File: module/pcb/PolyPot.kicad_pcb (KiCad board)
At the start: 2 copper layers, 50 x 50 mm, 40 parts, among them J1 V_BAT_1S, J2 PROG/DEBUG, J3 HUMIDITY_CONN, J4 TOF_DIST_SENS, J5 M3, J6 M3, J7 M3, J8 M3, J9 LUMINOSITY_CONN, M1 DC_WATER_PUMP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

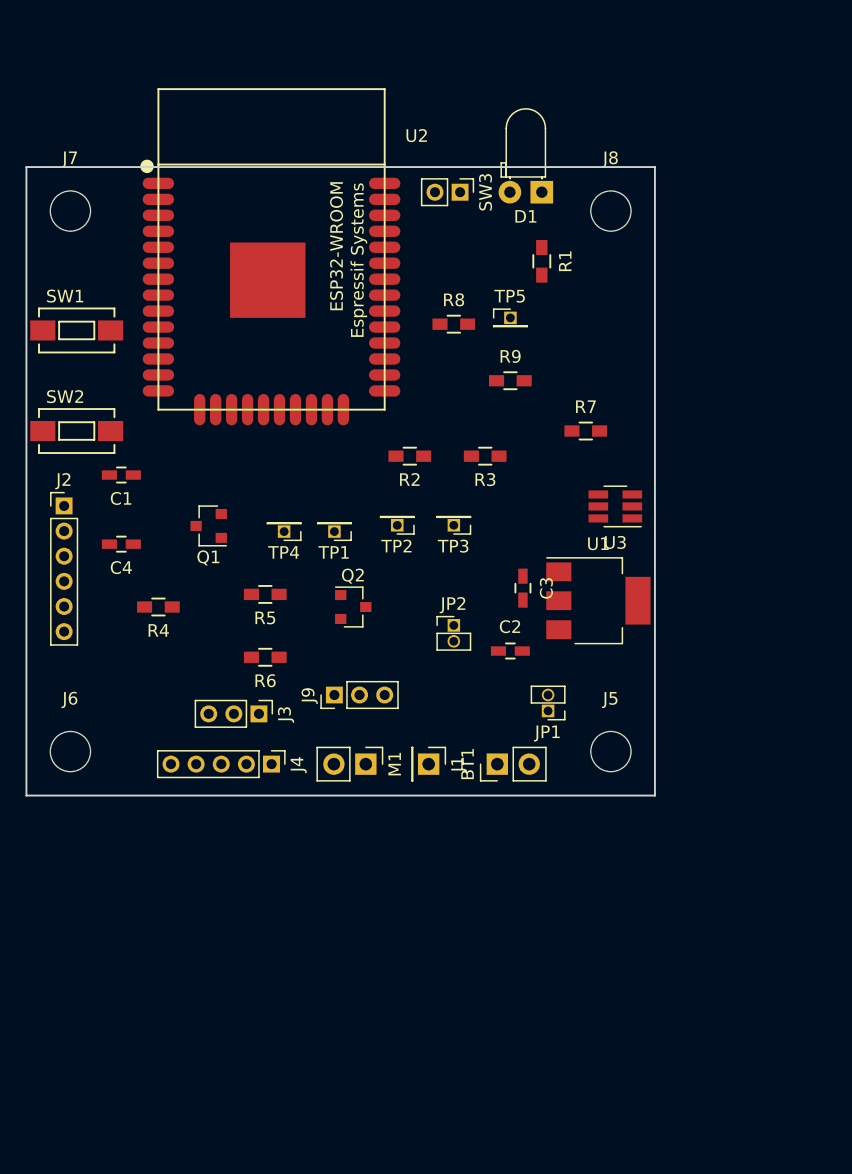
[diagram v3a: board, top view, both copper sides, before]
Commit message: First PCB routage+ small correction int the schematics
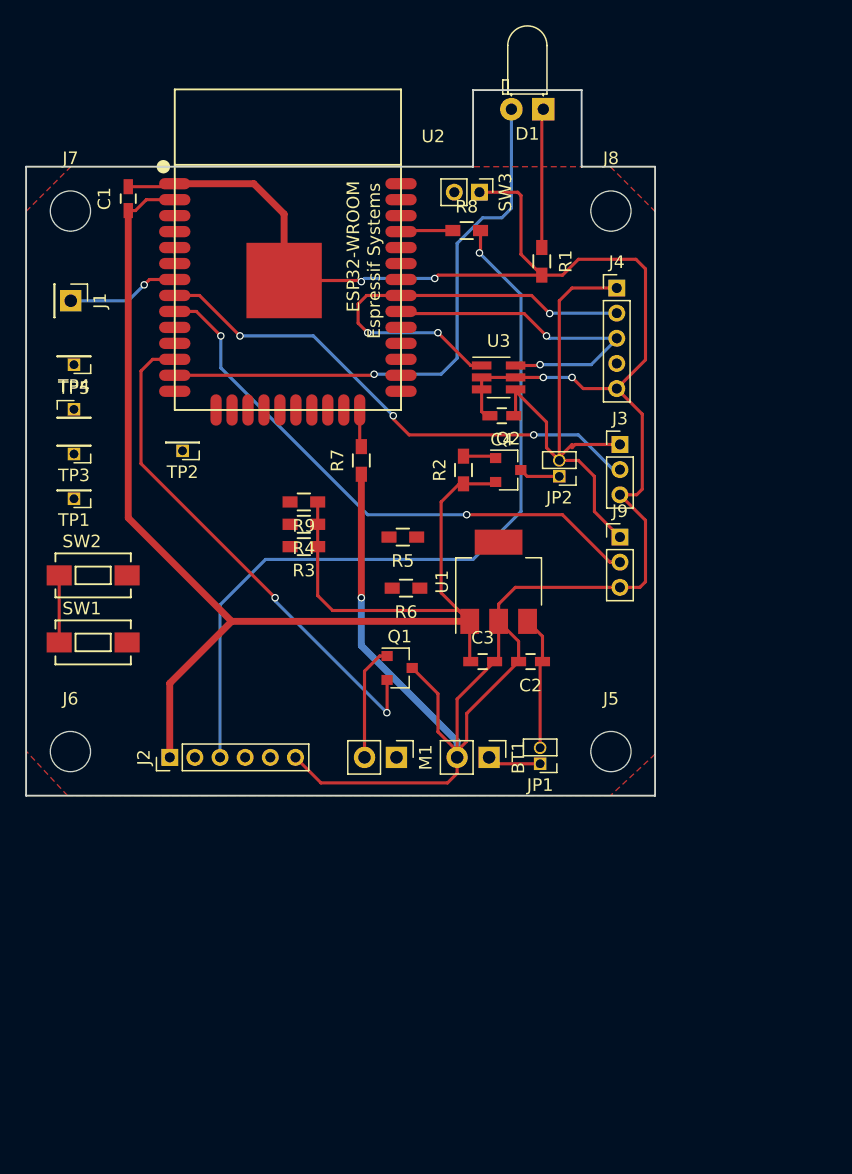
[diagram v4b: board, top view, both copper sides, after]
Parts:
- moved J4 46.8 mm to (77.0, 39.6), turned to 0 degrees
- moved J1 46.6 mm to (33.5, 40.6)
- moved J3 35.8 mm to (77.2, 52.1), turned to 0 degrees
- moved TP5 35.5 mm to (33.8, 49.3)
- moved C4 31.9 mm to (67.8, 49.8)
- moved TP3 30.7 mm to (33.8, 52.8)
- moved J9 26.0 mm to (77.2, 59.4), turned to 0 degrees
- moved SW1 24.9 mm to (35.3, 67.8)
- moved C1 22.0 mm to (38.1, 32.5), turned to 90 degrees
- moved J2 21.7 mm to (41.4, 77.0), turned to 90 degrees
- moved TP4 21.4 mm to (33.8, 45.7)
- moved TP1 20.9 mm to (33.8, 56.4)
- moved R9 19.1 mm to (52.1, 56.6), turned to 180 degrees
- moved Q1 18.9 mm to (59.7, 69.8), turned to 0 degrees
- moved TP2 18.1 mm to (42.4, 52.6)
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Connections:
- J4 pad 4: (no net) -> /TOF_GPIO0
- J5 pad 1: (no net) -> Net-(J5-Pad1)
- J6 pad 1: (no net) -> Net-(J6-Pad1)
- J7 pad 1: (no net) -> Net-(J7-Pad1)
- J8 pad 1: (no net) -> Net-(J8-Pad1)
- M1 pad 1: (no net) -> +BATT
- R3 pad 1: (no net) -> +3V3
- U2 pad 10: (no net) -> /USER_BTN
- U2 pad 11: (no net) -> Net-(U2-Pad11)
- U2 pad 15: (no net) -> Net-(U2-Pad15)
- U2 pad 16: (no net) -> Net-(U2-Pad16)
- U2 pad 17: (no net) -> Net-(U2-Pad17)
- U2 pad 18: (no net) -> Net-(U2-Pad18)
- U2 pad 19: (no net) -> Net-(U2-Pad19)
- U2 pad 20: (no net) -> Net-(U2-Pad20)
- U2 pad 21: (no net) -> Net-(U2-Pad21)
- U2 pad 22: (no net) -> Net-(U2-Pad22)
- U2 pad 23: (no net) -> Net-(U2-Pad23)
- U2 pad 26: (no net) -> Net-(U2-Pad26)
- U2 pad 27: (no net) -> Net-(U2-Pad27)
- U2 pad 28: (no net) -> Net-(U2-Pad28)
- U2 pad 29: (no net) -> Net-(U2-Pad29)
- U2 pad 32: (no net) -> Net-(U2-Pad32)
- U2 pad 33: (no net) -> Net-(U2-Pad33)
- U2 pad 36: (no net) -> Net-(U2-Pad36)
- U2 pad 37: (no net) -> Net-(U2-Pad37)
- U2 pad 38: (no net) -> Net-(U2-Pad38)
- U2 pad 4: (no net) -> Net-(U2-Pad4)
- U2 pad 5: (no net) -> Net-(U2-Pad5)
- U2 pad 6: (no net) -> Net-(U2-Pad6)
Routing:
- net GND: track 0.00 -> 196.6 mm, vias 0 -> 5
- net +3V3: track 0.00 -> 111.0 mm
- net /UART_TX: track 0.00 -> 62.9 mm, vias 0 -> 1
- net /LED_STATUS: track 0.00 -> 45.5 mm, vias 0 -> 1
- net /SENS_LUMINOSITY: track 0.00 -> 45.2 mm, vias 0 -> 2
- net /3V3_SENSORS: track 0.00 -> 41.8 mm
- net /SENS_HUMIDITY: track 0.00 -> 41.3 mm, vias 0 -> 3
- net /PUMP_PWM: track 0.00 -> 41.0 mm, vias 0 -> 2
- net /I2C_SCL: track 0.00 -> 34.2 mm, vias 0 -> 3
- net /I2C_SDA: track 0.00 -> 27.0 mm, vias 0 -> 2
- net Net-(D1-Pad1): track 0.00 -> 11.0 mm
- net Net-(C2-Pad1): track 0.00 -> 10.6 mm
- net Net-(M1-Pad2): track 0.00 -> 9.15 mm
- net /V_BAT_SENSE: track 0.00 -> 8.97 mm, vias 0 -> 1
- net Net-(BT1-Pad1): track 0.00 -> 4.27 mm
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- added copper zone on F.Cu, net GND
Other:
- board size 50 x 50 mm -> 50 x 56.1 mm
- net class Default: clearance 0.2 -> 0.36
- net class Signals added: clearance 0.36, trace_width 0.25, via_dia 0.6, via_drill 0.4
- rule trace_clearance: 0.2 -> 0.36

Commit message: PCB routage (except for track width to modify)
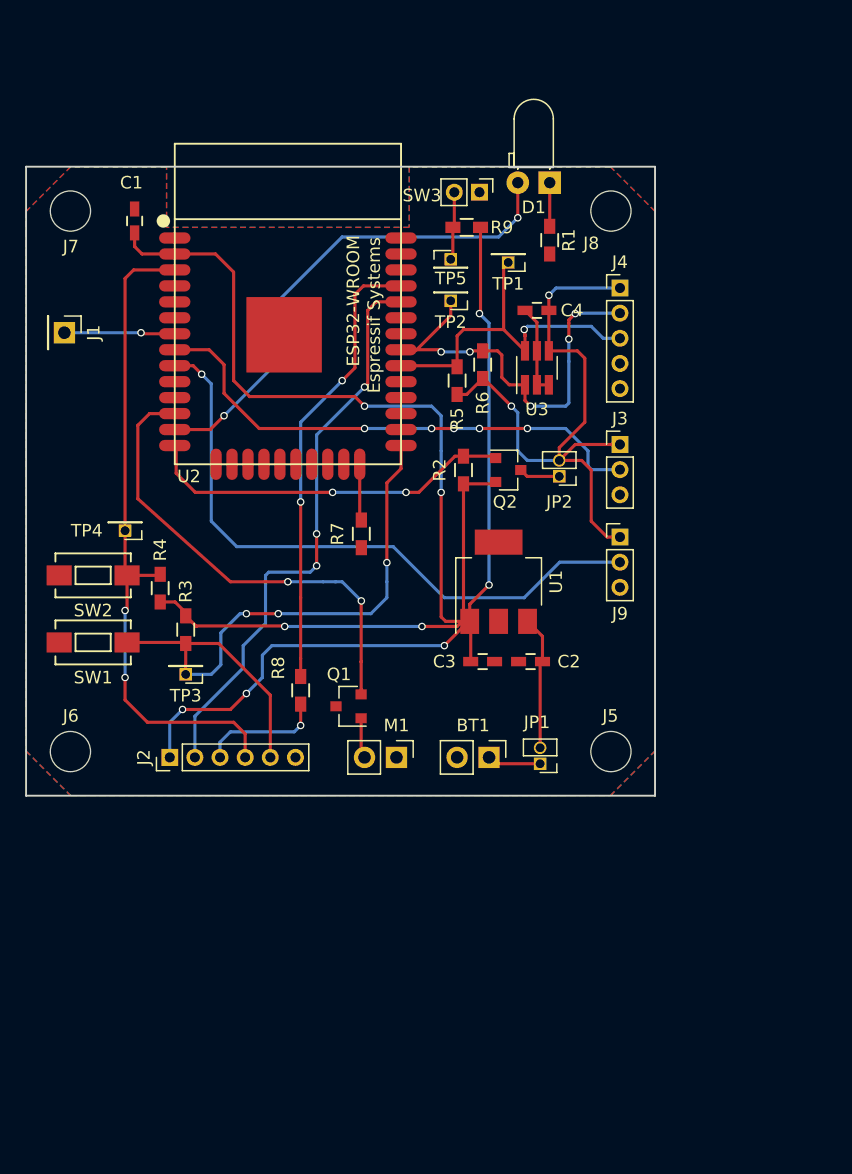
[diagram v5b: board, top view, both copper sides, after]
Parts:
- moved TP1 39.3 mm to (68.3, 37.6)
- moved R8 38.9 mm to (51.8, 71.6), turned to 270 degrees
- moved TP5 32.3 mm to (63.8, 37.3)
- moved R9 25.4 mm to (65.0, 34.8)
- moved TP2 24.4 mm to (63.8, 40.6)
- moved TP3 19.7 mm to (42.7, 70.4)
- moved R6 18.8 mm to (66.3, 45.7), turned to 90 degrees
- moved TP4 13.8 mm to (37.8, 58.9)
- moved R5 13.2 mm to (64.3, 47.0), turned to 90 degrees
- moved R4 12.5 mm to (40.6, 63.5), turned to 90 degrees
- moved R3 11.5 mm to (42.7, 66.8), turned to 270 degrees
- moved C4 8.84 mm to (70.6, 41.4)
- moved D1 5.86 mm to (71.6, 31.2)
- moved R7 5.84 mm to (56.6, 59.2)
- moved Q1 5.08 mm to (55.6, 72.9), turned to 180 degrees
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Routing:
- net GND: track 196.6 -> 7.27 mm, vias 5 -> 0
- net /GPIO0: track 0.00 -> 53.2 mm, vias 0 -> 3
- net /EN: track 0.00 -> 53.2 mm, vias 0 -> 2
- net /UART_TX: track 62.9 -> 9.96 mm
- net +3V3: track 111.0 -> 160.7 mm, vias 0 -> 9
- net /UART_RX: track 0.00 -> 46.1 mm, vias 0 -> 3
- net Net-(R8-Pad1): track 4.16 -> 36.1 mm, vias 0 -> 2
- net /SENSORS_ENn: track 2.62 -> 29.5 mm, vias 0 -> 2
- net /3V3_SENSORS: track 41.8 -> 50.7 mm, vias 0 -> 2
- net Net-(D1-Pad1): track 11.0 -> 3.47 mm
- net Net-(M1-Pad2): track 9.15 -> 3.23 mm
- net /LED_STATUS: track 45.5 -> 40.0 mm, vias 1 -> 2
- net /SENS_LUMINOSITY: track 45.2 -> 50.6 mm, vias 2 -> 1
- net /USER_BUTTON: track 0.00 -> 5.45 mm
- net /PUMP_PWM: track 41.0 -> 37.9 mm
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- added copper zone on B.Cu, net GND
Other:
- board size 50 x 56.1 mm -> 50 x 50 mm
- net class Default: clearance 0.36 -> 0.3
- net class Signals removed
- rule trace_clearance: 0.36 -> 0.3

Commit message: New routing using the ESP32-S footprint
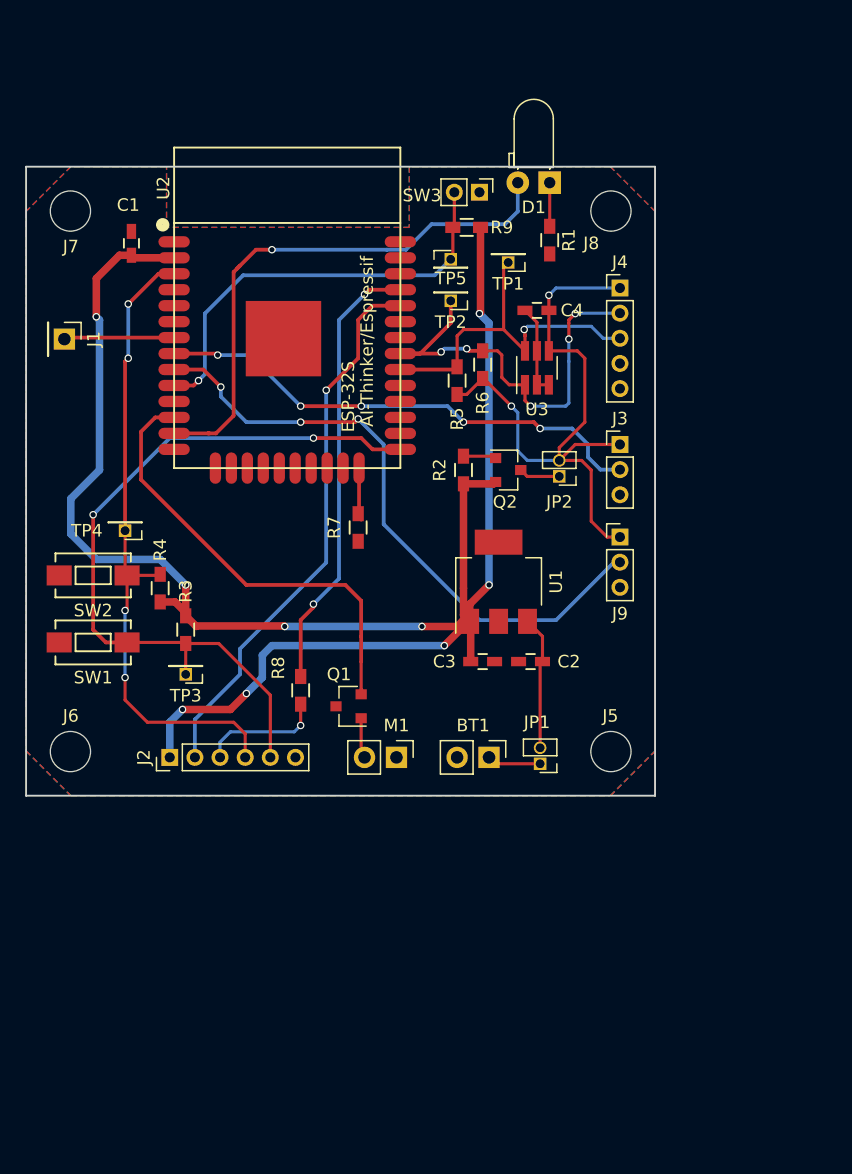
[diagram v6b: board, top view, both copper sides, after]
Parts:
- U2: value ESP32-WROOM -> ESP-32S; footprint PolyPot:ESP32-WROOM -> ESP32-footprints-Lib:ESP-32S
- moved U2 4.57 mm to (50.8, 45.5), turned to 0 degrees
- moved C1 1.80 mm to (38.4, 36.1)
- moved R7 0.57 mm to (56.4, 58.7)
- moved J1 0.51 mm to (33.0, 43.7)
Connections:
- R9 pad 2: /USER_BUTTON -> /USER_BTN
- SW3 pad 2: /USER_BUTTON -> /USER_BTN
- TP5 pad 1: /USER_BUTTON -> /USER_BTN
- U2 pad 14: /SENSORS_ENn -> /SENSOR_ENn
- U2 pad 15: Net-(U2-Pad15) -> GND
- U2 pad 38: Net-(U2-Pad38) -> GND
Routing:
- net /USER_BTN: track 0.00 -> 34.4 mm, vias 0 -> 1
- net /SENSORS_ENn: track 29.5 -> 2.62 mm, vias 2 -> 0
- net +3V3: track 160.7 -> 147.8 mm
- net /GPIO0: track 53.2 -> 60.3 mm, vias 3 -> 2
- net /USER_BUTTON: track 5.45 -> 0.00 mm
- net /LED_STATUS: track 40.0 -> 44.1 mm, vias 2 -> 1
- net /UART_RX: track 46.1 -> 44.0 mm, vias 3 -> 1
- net /PUMP_PWM: track 37.9 -> 36.3 mm, vias 2 -> 0
- net /SENS_HUMIDITY: track 41.4 -> 39.9 mm
- net /EN: track 53.2 -> 51.7 mm, vias 2 -> 4
- net /I2C_SCL: track 34.4 -> 35.1 mm
- net Net-(R7-Pad2): track 4.49 -> 3.84 mm
- net Net-(R8-Pad1): track 36.1 -> 35.5 mm
- net /SENS_LUMINOSITY: track 50.6 -> 50.0 mm, vias 1 -> 3
- net /V_BAT_SENSE: track 8.81 -> 8.78 mm, vias 1 -> 0
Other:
- net class Power added: clearance 0.3, trace_width 0.6, via_dia 0.6, via_drill 0.4
- net class Signals added: clearance 0.3, trace_width 0.3, via_dia 0.6, via_drill 0.4

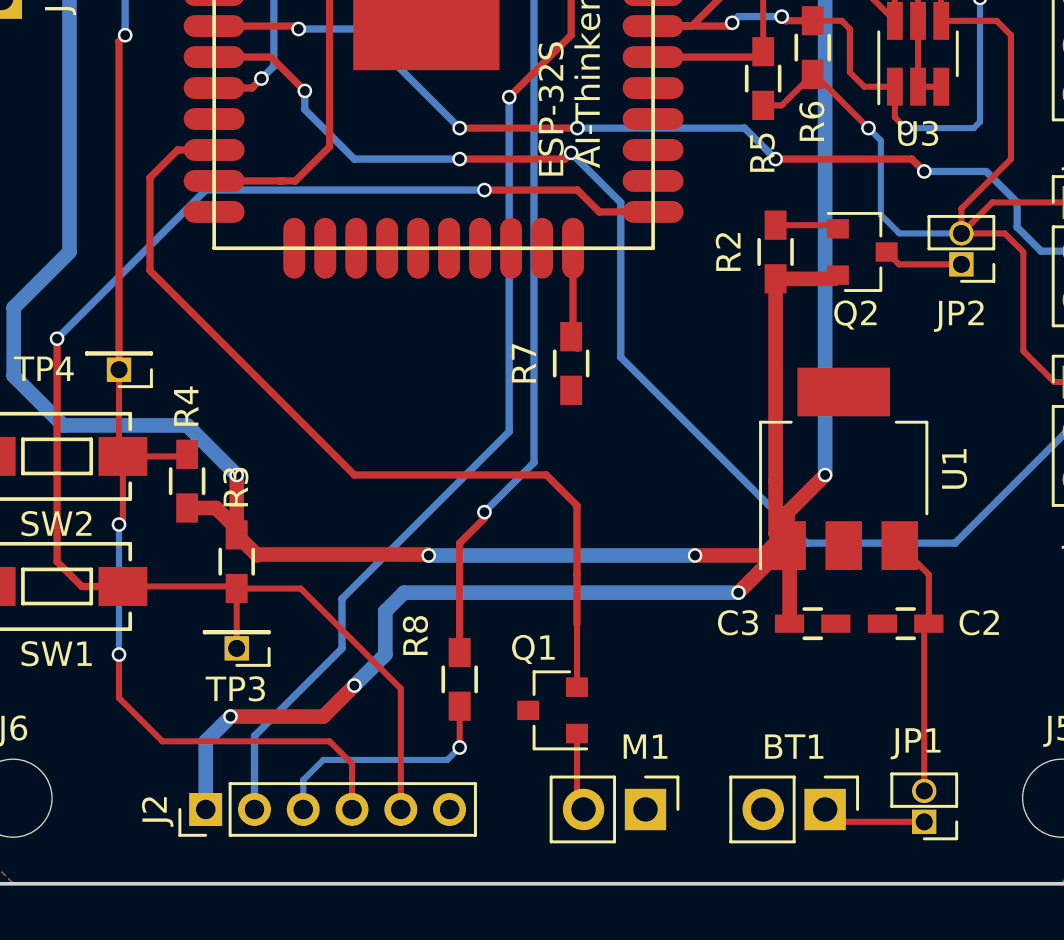
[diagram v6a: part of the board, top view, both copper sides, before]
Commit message: Added the PWM driver and routed it on the PCB
There might be some issues with the path for library for ESP32-S. You might need to respecify the path to "ESP32-footprints-Lib.pretty" in the PCB editor library manager.
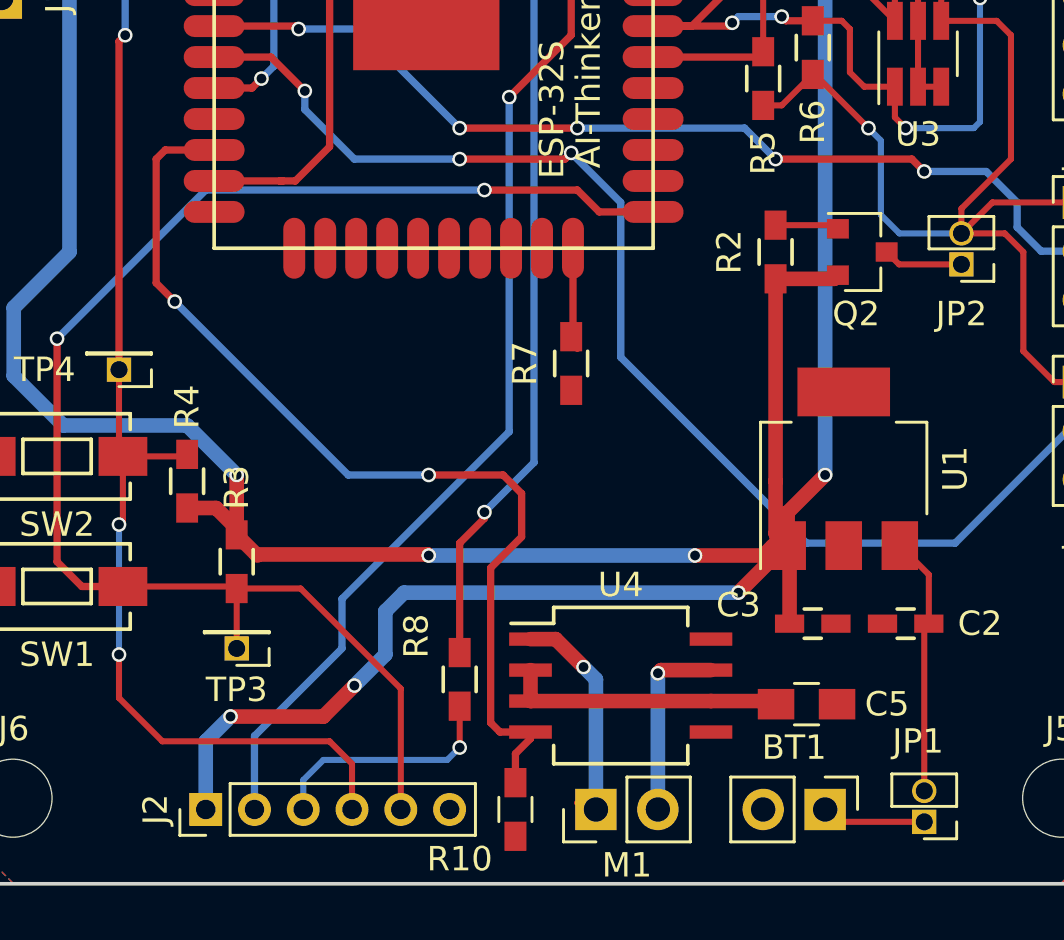
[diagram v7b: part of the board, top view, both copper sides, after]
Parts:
- removed Q1: Q_NMOS_DGS, TO_SOT_Packages_SMD:SOT-23
- added C5: 10uF, Capacitors_SMD:C_0805_HandSoldering, F.Cu at (66.0, 72.6)
- added R10: 10k, Resistors_SMD:R_0603_HandSoldering, F.Cu at (54.1, 77.0)
- added U4: BD6211F-E2, Housings_SOIC:SO-8_5.3x6.2mm_Pitch1.27mm, F.Cu at (58.4, 71.9)
- moved M1 2.03 mm to (57.4, 77.0), turned to 90 degrees
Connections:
- M1 pad 1: +BATT -> Net-(M1-Pad1)
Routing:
- net /+BATT: track 0.00 -> 11.4 mm
- net Net-(M1-Pad1): track 0.00 -> 9.08 mm, vias 0 -> 1
- net Net-(M1-Pad2): track 3.23 -> 7.82 mm, vias 0 -> 1
- net /PUMP_PWM: track 36.3 -> 40.2 mm, vias 0 -> 2
